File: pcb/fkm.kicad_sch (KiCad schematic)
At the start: 14 parts, among them U1 ESP32-WROOM-32, U2 18650, U3 AMS1117-3.3

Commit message: feat(pcb): decoupling capacitor
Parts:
- added C1: C, Capacitor_SMD:C_0805_2012Metric_Pad1.18x1.45mm_HandSolder, symbol Device:C
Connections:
- net +3.3V: now also C1.2
- net GND: now also C1.1
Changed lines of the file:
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@@
+	)
+	(symbol
+		(lib_name "GND_2")
+		(lib_id "power:GND")
+		(at 96.52 46.99 0)
+		(unit 1)
+		(exclude_from_sim no)
+		(in_bom yes)
+		(on_board yes)
+		(dnp no)
+		(fields_autoplaced yes)
+		(property "Reference" "#PWR010"
+			(at 96.52 53.34 0)
+			(effects
+				(font
+					(size 1.27 1.27)
+				)
+				(hide yes)
+			)
+		)
+		(property "Value" "GND"
+			(at 96.52 52.07 0)
+			(effects
+				(font
+					(size 1.27 1.27)
+				)
+			)
+		)
+		(property "Footprint" ""
+			(at 96.52 46.99 0)
+			(effects
+				(font
+					(size 1.27 1.27)
+				)
+				(hide yes)
+			)
+		)
+		(property "Datasheet" ""
+			(at 96.52 46.99 0)
+			(effects
+				(font
+					(size 1.27 1.27)
+				)
+				(hide yes)
+			)
+		)
+		(property "Description" "Power symbol creates a global label with name \"GND\" , ground"
+			(at 96.52 46.99 0)
+			(effects
+				(font
+					(size 1.27 1.27)
+				)
+				(hide yes)
+			)
+		)
+		(pin "1"
+		)
+		(instances
+			(project "fkm"
+				(path "/ccd0dcac-df1d-4089-8f7e-e62a3e2f6f2a"
+					(reference "#PWR010")
+					(unit 1)
+				)
+			)
+		)
 	)
 	(symbol
@@
 	)
 	(symbol
+		(lib_id "Device:C")
+		(at 96.52 43.18 180)
+		(unit 1)
+		(exclude_from_sim no)
+		(in_bom yes)
+		(on_board yes)
+		(dnp no)
+		(fields_autoplaced yes)
+		(property "Reference" "C1"
+			(at 100.33 41.9099 0)
+			(effects
+				(font
+					(size 1.27 1.27)
+				)
+				(justify right)
+			)
+		)
+		(property "Value" "C"
+			(at 100.33 44.4499 0)
+			(effects
+				(font
+					(size 1.27 1.27)
+				)
+				(justify right)
+			)
+		)
+		(property "Footprint" "Capacitor_SMD:C_0805_2012Metric_Pad1.18x1.45mm_HandSolder"
+			(at 95.5548 39.37 0)
+			(effects
+				(font
+					(size 1.27 1.27)
+				)
+				(hide yes)
+			)
+		)
+		(property "Datasheet" "~"
+			(at 96.52 43.18 0)
+			(effects
+				(font
+					(size 1.27 1.27)
+				)
+				(hide yes)
+			)
+		)
+		(property "Description" "Unpolarized capacitor"
+			(at 96.52 43.18 0)
+			(effects
+				(font
+					(size 1.27 1.27)
+				)
+				(hide yes)
+			)
+		)
+		(pin "1"
+		)
+		(pin "2"
+		)
+		(instances
+			(project "fkm"
+				(path "/ccd0dcac-df1d-4089-8f7e-e62a3e2f6f2a"
+					(reference "C1")
+					(unit 1)
+				)
+			)
+		)
+	)
+	(symbol
 		(lib_id "power:GND")
 		(at 118.11 113.03 270)
@@
 					(unit 1)
 				)
+			)
+		)
+	)
+	(symbol
+		(lib_name "+3.3V_2")
+		(lib_id "power:+3.3V")
+		(at 96.52 39.37 0)
+		(unit 1)
+		(exclude_from_sim no)
+		(in_bom yes)
+		(on_board yes)
+		(dnp no)
+		(fields_autoplaced yes)
+		(property "Reference" "#PWR09"
+			(at 96.52 43.18 0)
+			(effects
+				(font
+					(size 1.27 1.27)
+				)
+				(hide yes)
+			)
+		)
+		(property "Value" "+3.3V"
+			(at 96.52 34.29 0)
+			(effects
+				(font
+					(size 1.27 1.27)
+				)
+			)
+		)
+		(property "Footprint" ""
+			(at 96.52 39.37 0)
+			(effects
+				(font
+					(size 1.27 1.27)
+				)
+				(hide yes)
+			)
+		)
+		(property "Datasheet" ""
+			(at 96.52 39.37 0)
+			(effects
+				(font
+					(size 1.27 1.27)
+				)
+				(hide yes)
+			)
+		)
+		(property "Description" "Power symbol creates a global label with name \"+3.3V\""
+			(at 96.52 39.37 0)
+			(effects
+				(font
+					(size 1.27 1.27)
+				)
+				(hide yes)
+			)
+		)
+		(pin "1"
+		)
+		(instances
+			(project "fkm"
+				(path "/ccd0dcac-df1d-4089-8f7e-e62a3e2f6f2a"
+					(reference "#PWR09")
+					(unit 1)
+				)

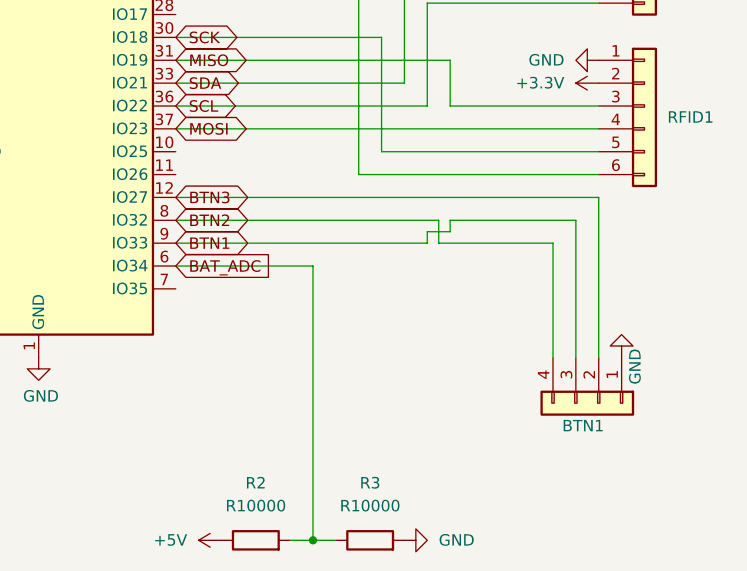
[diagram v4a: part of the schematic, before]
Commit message: feat(pcb): 4xbuttons output
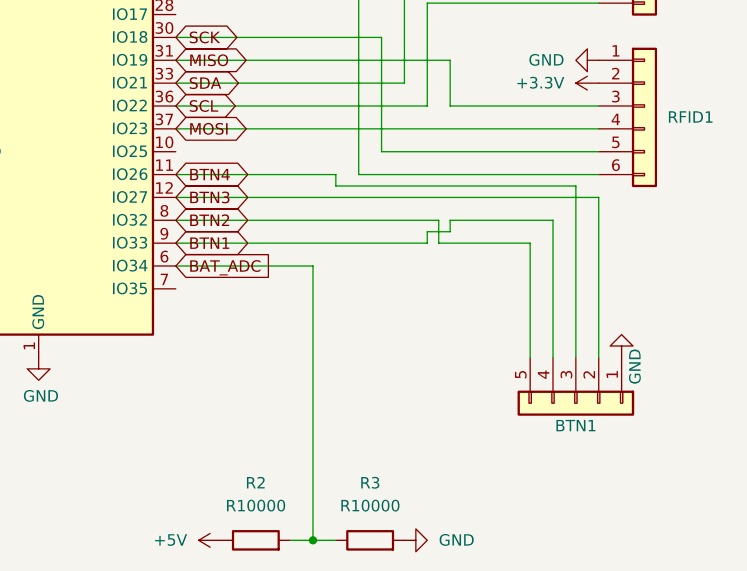
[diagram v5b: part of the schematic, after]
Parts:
- removed BTN1: Conn_01x04, Connector_PinHeader_2.54mm:PinHeader_1x04_P2.54mm_Vertical, symbol Connector_Generic:Conn_01x04
- added BTN1: Conn_01x05, Connector_PinHeader_2.54mm:PinHeader_1x05_P2.54mm_Vertical, symbol Connector_Generic:Conn_01x05
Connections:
- net BTN1: now also BTN1.4 (Pin_4)
- net BTN2: now also BTN1.5 (Pin_5)
- net BTN3: now also BTN1.2 (Pin_2)
- net GND: now also BTN1.1 (Pin_1)
- net BTN4: now reaches U1.11 (IO26)
- net BTN4: now also BTN1.3 (Pin_3)
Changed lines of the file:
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@@
+	(wire
+		(pts
+			(xy 101.6 151.13) (xy 113.03 151.13)
+		)
+		(stroke
+			(width 0)
+			(type default)
+		)
+	)
 	(wire
 		(pts
@@
 	(wire
 		(pts
-			(xy 113.03 153.67) (xy 113.03 166.37)
-		)
-		(stroke
-			(width 0)
-			(type default)
-		)
-	)
-	(wire
-		(pts
 			(xy 55.88 86.36) (xy 55.88 95.25)
 		)
@@
 	(wire
 		(pts
-			(xy 113.03 153.67) (xy 100.33 153.67)
+			(xy 115.57 147.32) (xy 115.57 166.37)
 		)
 		(stroke
@@
 	(wire
 		(pts
+			(xy 88.9 147.32) (xy 115.57 147.32)
+		)
+		(stroke
+			(width 0)
+			(type default)
+		)
+	)
+	(wire
+		(pts
 			(xy 38.1 48.26) (xy 45.72 48.26)
 		)
@@
 	(wire
 		(pts
+			(xy 71.12 146.05) (xy 88.9 146.05)
+		)
+		(stroke
+			(width 0)
+			(type default)
+		)
+	)
+	(wire
+		(pts
 			(xy 91.44 99.06) (xy 92.71 99.06)
 		)
@@
 	(wire
 		(pts
+			(xy 113.03 151.13) (xy 113.03 166.37)
+		)
+		(stroke
+			(width 0)
+			(type default)
+		)
+	)
+	(wire
+		(pts
 			(xy 40.64 93.98) (xy 40.64 100.33)
 		)
@@
 	(wire
 		(pts
+			(xy 110.49 153.67) (xy 110.49 166.37)
+		)
+		(stroke
+			(width 0)
+			(type default)
+		)
+	)
+	(wire
+		(pts
 			(xy 101.6 133.35) (xy 101.6 138.43)
 		)
@@
 	(wire
 		(pts
-			(xy 115.57 151.13) (xy 115.57 166.37)
-		)
-		(stroke
-			(width 0)
-			(type default)
-		)
-	)
-	(wire
-		(pts
 			(xy 58.42 57.15) (xy 60.96 57.15)
 		)
@@
 	(wire
 		(pts
+			(xy 100.33 153.67) (xy 110.49 153.67)
+		)
+		(stroke
+			(width 0)
+			(type default)
+		)
+	)
+	(wire
+		(pts
 			(xy 114.3 115.57) (xy 114.3 110.49)
 		)
@@
 	(wire
 		(pts
+			(xy 88.9 146.05) (xy 88.9 147.32)
+		)
+		(stroke
+			(width 0)
+			(type default)
+		)
+	)
+	(wire
+		(pts
 			(xy 86.36 93.98) (xy 96.52 93.98)
 		)
@@
 		(pts
 			(xy 93.98 99.06) (xy 96.52 99.06)
-		)
-		(stroke
-			(width 0)
-			(type default)
-		)
-	)
-	(wire
-		(pts
-			(xy 115.57 151.13) (xy 101.6 151.13)
 		)
 		(stroke
@@
 		(property "Intersheetrefs" "${INTERSHEET_REFS}"
 			(at 71.12 156.21 0)
+			(effects
+				(font
+					(size 1.27 1.27)
+				)
+				(hide yes)
+			)
+		)
+	)
+	(global_label "BTN4"
+		(shape bidirectional)
+		(at 71.12 146.05 0)
+		(effects
+			(font
+				(size 1.27 1.27)
+			)
+			(justify left)
+		)
+		(property "Intersheetrefs" "${INTERSHEET_REFS}"
+			(at 71.12 146.05 0)
 			(effects
 				(font
@@
 	)
 	(symbol
-		(lib_id "Connector_Generic:Conn_01x04")
-		(at 118.11 171.45 270)
-		(unit 1)
-		(exclude_from_sim no)
-		(in_bom yes)
-		(on_board yes)
-		(dnp no)
-		(property "Reference" "BTN1"
-			(at 114.046 173.99 90)
-			(effects
-				(font
-					(size 1.27 1.27)
-				)
-				(justify left)
-			)
-		)
-		(property "Value" "Conn_01x04"
-			(at 115.5701 173.99 0)
-			(effects
-				(font
-					(size 1.27 1.27)
-				)
-				(justify left)
-				(hide yes)
-			)
-		)
-		(property "Footprint" "Connector_PinHeader_2.54mm:PinHeader_1x04_P2.54mm_Vertical"
-			(at 118.11 171.45 0)
-			(effects
-				(font
-					(size 1.27 1.27)
-				)
-				(hide yes)
-			)
-		)
-		(property "Datasheet" "~"
-			(at 118.11 171.45 0)
-			(effects
-				(font
-					(size 1.27 1.27)
-				)
-				(hide yes)
-			)
-		)
-		(property "Description" "Generic connector, single row, 01x04, script generated (kicad-library-utils/schlib/autogen/connector/)"
-			(at 118.11 171.45 0)
-			(effects
-				(font
-					(size 1.27 1.27)
-				)
-				(hide yes)
-			)
-		)
-		(pin "2"
-		)
-		(pin "1"
-		)
-		(pin "3"
-		)
-		(pin "4"
-		)
-		(instances
-			(project "fkm"
-				(path "/ccd0dcac-df1d-4089-8f7e-e62a3e2f6f2a"
-					(reference "BTN1")
-					(unit 1)
-				)
-			)
-		)
-	)
-	(symbol
 		(lib_name "+5V_1")
 		(lib_id "power:+5V")
@@
 					(unit 1)
 				)
+			)
+		)
+	)
+	(symbol
+		(lib_id "Connector_Generic:Conn_01x05")
+		(at 115.57 171.45 270)
+		(unit 1)
+		(exclude_from_sim no)
+		(in_bom yes)
+		(on_board yes)
+		(dnp no)
+		(property "Reference" "BTN1"
+			(at 115.57 173.99 90)
+			(effects
+				(font
+					(size 1.27 1.27)
+				)
+			)
+		)
+		(property "Value" "Conn_01x05"
+			(at 115.57 177.8 90)
+			(effects
+				(font
+					(size 1.27 1.27)
+				)
+				(hide yes)
+			)
+		)
+		(property "Footprint" "Connector_PinHeader_2.54mm:PinHeader_1x05_P2.54mm_Vertical"
+			(at 115.57 171.45 0)
+			(effects
+				(font
+					(size 1.27 1.27)
+				)
+				(hide yes)
+			)
+		)
+		(property "Datasheet" "~"
+			(at 115.57 171.45 0)
+			(effects
+				(font
+					(size 1.27 1.27)
+				)
+				(hide yes)
+			)
+		)
+		(property "Description" "Generic connector, single row, 01x05, script generated (kicad-library-utils/schlib/autogen/connector/)"
+			(at 115.57 171.45 0)
+			(effects
+				(font
+					(size 1.27 1.27)
+				)
+				(hide yes)
+			)
+		)
+		(pin "4"
+		)
+		(pin "3"
+		)
+		(pin "2"
+		)
+		(pin "1"
+		)
+		(pin "5"
+		)
+		(instances
+			(project "fkm"
+				(path "/ccd0dcac-df1d-4089-8f7e-e62a3e2f6f2a"
+					(reference "BTN1")
+					(unit 1)
+				)

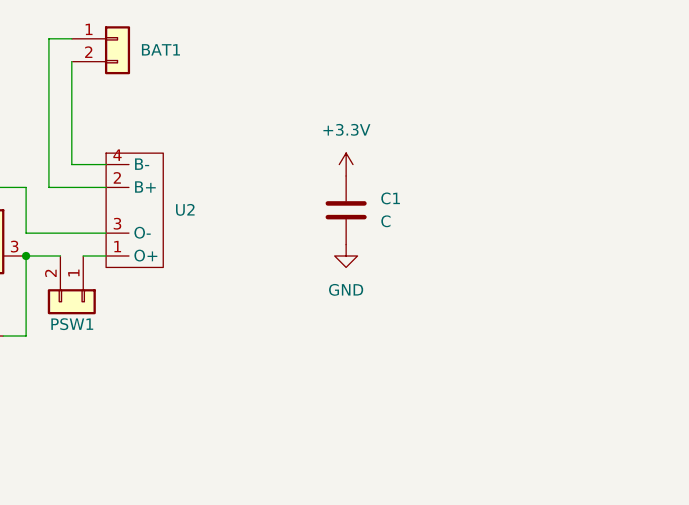
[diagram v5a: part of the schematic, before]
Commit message: chore: pcb decoupling capacitor value
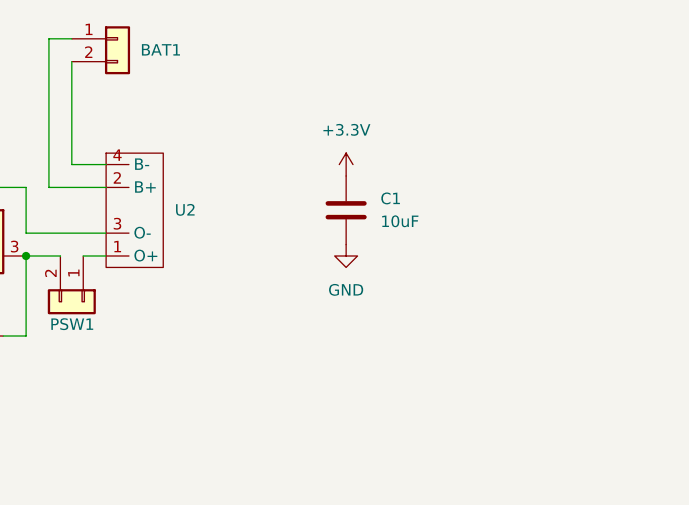
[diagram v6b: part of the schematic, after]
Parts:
- C1: value C -> 10uF
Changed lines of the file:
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@@
 			)
 		)
-		(property "Value" "C"
+		(property "Value" "10uF"
 			(at 100.33 44.4499 0)
 			(effects
